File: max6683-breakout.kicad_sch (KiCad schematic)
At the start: 12 parts, among them J1 Conn_01x05, J2 Conn_01x05, U1 MAX6683

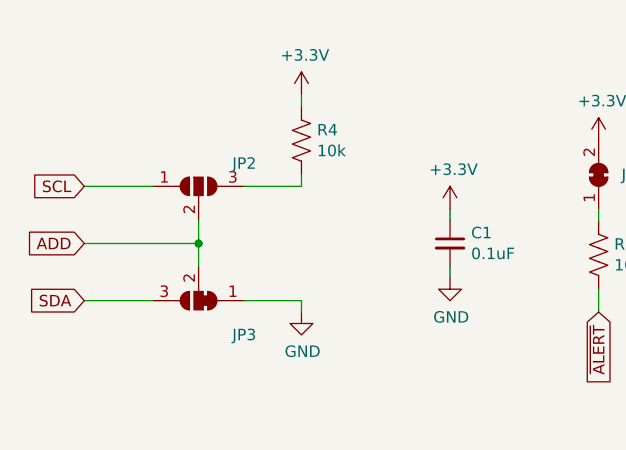
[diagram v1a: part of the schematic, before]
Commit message: Update PCB to eliminate clearance DRC issues
Supports #44.
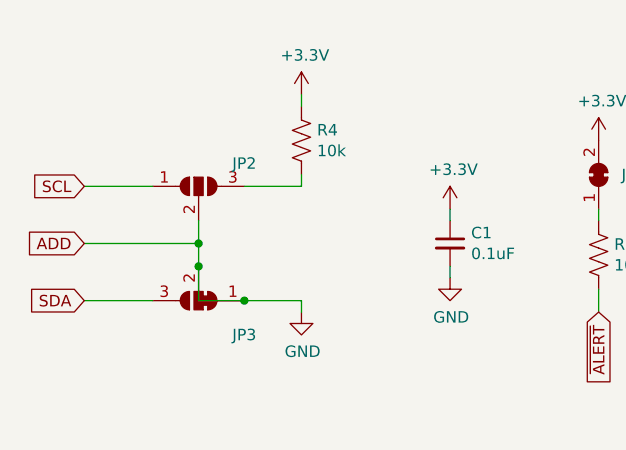
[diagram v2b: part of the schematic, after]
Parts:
- JP3: footprint Jumper:SolderJumper-3_P1.3mm_Bridged12_RoundedPad1.0x1.5mm -> Jumper:SolderJumper-3_P1.3mm_Open_RoundedPad1.0x1.5mm
- JP4: value (none) -> SolderJumper_2_Bridged; footprint (none) -> Jumper:SolderJumper-2_P1.3mm_Bridged_RoundedPad1.0x1.5mm
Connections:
- net ADD is gone; now on net GND: J2.2 (Pin_2), JP2.2 (C), JP3.2 (C), U1.7 (ADD)
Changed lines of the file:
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@@
   (junction (at 158.75 78.74) (diameter 0) (color 0 0 0 0)
   )
+  (junction (at 123.19 125.73) (diameter 0) (color 0 0 0 0)
+  )
   (junction (at 121.92 86.36) (diameter 0) (color 0 0 0 0)
+  )
+  (junction (at 118.11 121.92) (diameter 0) (color 0 0 0 0)
   )
   (no_connect (at 119.38 83.82))
@@
     (stroke (width 0) (type default) (color 0 0 0 0))
   )
+  (wire (pts (xy 118.11 125.73) (xy 118.11 121.92))
+    (stroke (width 0) (type default) (color 0 0 0 0))
+  )
   (wire (pts (xy 123.19 125.73) (xy 129.54 125.73))
     (stroke (width 0) (type default) (color 0 0 0 0))
@@
   )
   (wire (pts (xy 147.32 86.36) (xy 173.99 86.36))
+    (stroke (width 0) (type default) (color 0 0 0 0))
+  )
+  (wire (pts (xy 123.19 125.73) (xy 118.11 125.73))
     (stroke (width 0) (type default) (color 0 0 0 0))
   )
@@
       (effects (font (size 1.27 1.27)) hide)
     )
-    (property "Footprint" "Jumper:SolderJumper-3_P1.3mm_Bridged12_RoundedPad1.0x1.5mm" (id 2) (at 118.11 125.73 0)
+    (property "Footprint" "Jumper:SolderJumper-3_P1.3mm_Open_RoundedPad1.0x1.5mm" (id 2) (at 118.11 125.73 0)
       (effects (font (size 1.27 1.27)) hide)
     )
@@
       (effects (font (size 1.27 1.27)) (justify right))
     )
-    (property "Value" "" (id 1) (at 158.75 111.76 0)
-      (effects (font (size 1.27 1.27)) hide)
-    )
-    (property "Footprint" "" (id 2) (at 162.56 111.76 0)
+    (property "Value" "SolderJumper_2_Bridged" (id 1) (at 158.75 111.76 0)
+      (effects (font (size 1.27 1.27)) hide)
+    )
+    (property "Footprint" "Jumper:SolderJumper-2_P1.3mm_Bridged_RoundedPad1.0x1.5mm" (id 2) (at 162.56 111.76 0)
       (effects (font (size 1.27 1.27)) hide)
     )
@@
     )
     (path "/0fa81537-8214-4df6-96f6-9377354bc47f"
-      (reference "JP3") (unit 1) (value "SolderJumper_3_Bridged12") (footprint "Jumper:SolderJumper-3_P1.3mm_Bridged12_RoundedPad1.0x1.5mm")
+      (reference "JP3") (unit 1) (value "SolderJumper_3_Bridged12") (footprint "Jumper:SolderJumper-3_P1.3mm_Open_RoundedPad1.0x1.5mm")
     )
     (path "/18b6dcb6-5ab3-481b-b998-33e8cf6d281f"

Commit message: Begin routing
Supports #44.
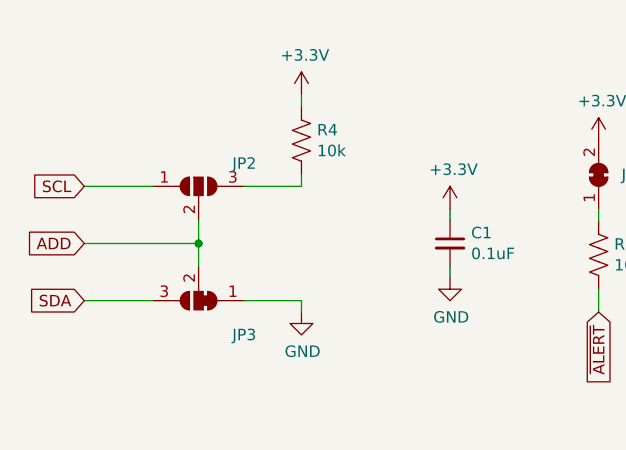
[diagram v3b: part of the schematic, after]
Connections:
- net GND: no longer J2.2 (Pin_2), JP2.2 (C), JP3.2 (C), U1.7 (ADD)
- new net ADD: J2.2 (Pin_2), JP2.2 (C), JP3.2 (C), U1.7 (ADD)
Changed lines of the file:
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@@
   (junction (at 158.75 78.74) (diameter 0) (color 0 0 0 0)
   )
-  (junction (at 123.19 125.73) (diameter 0) (color 0 0 0 0)
-  )
   (junction (at 121.92 86.36) (diameter 0) (color 0 0 0 0)
-  )
-  (junction (at 118.11 121.92) (diameter 0) (color 0 0 0 0)
   )
   (no_connect (at 119.38 83.82))
@@
     (stroke (width 0) (type default) (color 0 0 0 0))
   )
-  (wire (pts (xy 118.11 125.73) (xy 118.11 121.92))
-    (stroke (width 0) (type default) (color 0 0 0 0))
-  )
   (wire (pts (xy 123.19 125.73) (xy 129.54 125.73))
     (stroke (width 0) (type default) (color 0 0 0 0))
@@
     (stroke (width 0) (type default) (color 0 0 0 0))
   )
-  (wire (pts (xy 123.19 125.73) (xy 118.11 125.73))
-    (stroke (width 0) (type default) (color 0 0 0 0))
-  )

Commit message: Complete routing
Supports #44.
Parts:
- JP3: value SolderJumper_3_Bridged12 -> (none); footprint Jumper:SolderJumper-3_P1.3mm_Open_RoundedPad1.0x1.5mm -> (none)
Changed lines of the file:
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@@
     (in_bom no) (on_board yes)
     (property "Reference" "JP3" (id 0) (at 123.19 129.54 0))
-    (property "Value" "SolderJumper_3_Bridged12" (id 1) (at 118.11 129.54 0)
+    (property "Value" "" (id 1) (at 118.11 129.54 0)
       (effects (font (size 1.27 1.27)) hide)
     )
-    (property "Footprint" "Jumper:SolderJumper-3_P1.3mm_Open_RoundedPad1.0x1.5mm" (id 2) (at 118.11 125.73 0)
+    (property "Footprint" "" (id 2) (at 118.11 125.73 0)
       (effects (font (size 1.27 1.27)) hide)
     )
@@
     )
     (path "/0fa81537-8214-4df6-96f6-9377354bc47f"
-      (reference "JP3") (unit 1) (value "SolderJumper_3_Bridged12") (footprint "Jumper:SolderJumper-3_P1.3mm_Open_RoundedPad1.0x1.5mm")
+      (reference "JP3") (unit 1) (value "SolderJumper_3_Bridged12") (footprint "Jumper:SolderJumper-3_P1.3mm_Bridged12_RoundedPad1.0x1.5mm_NumberLabels")
     )
     (path "/18b6dcb6-5ab3-481b-b998-33e8cf6d281f"

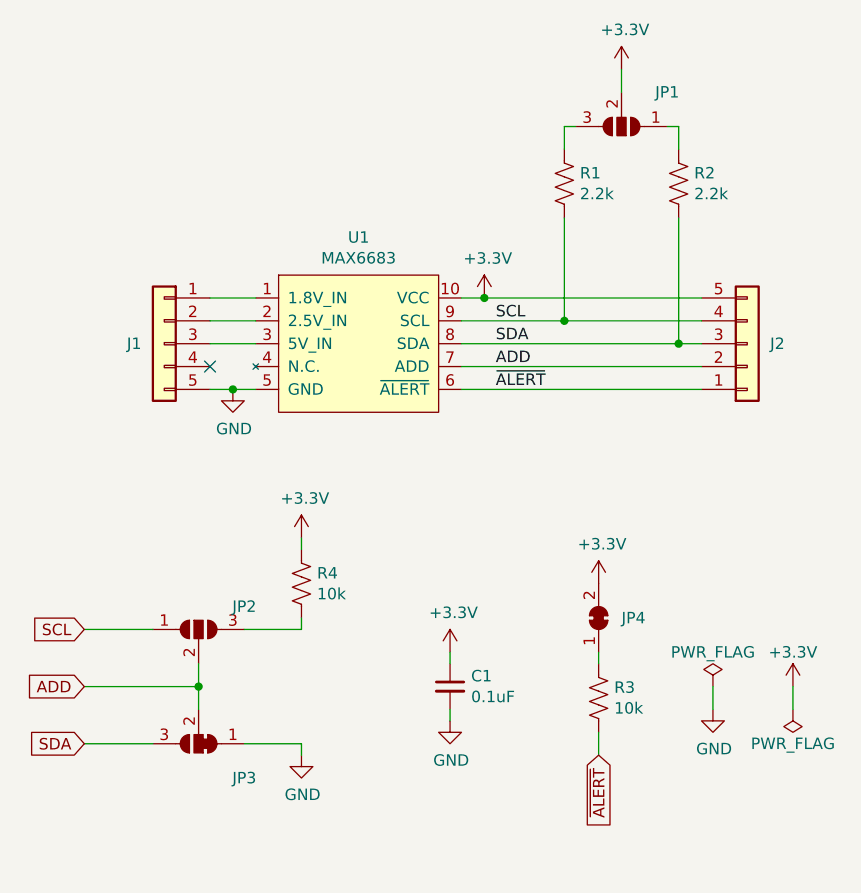
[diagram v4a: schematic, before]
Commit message: Inject ERC errors to test CI job
Supports #44.
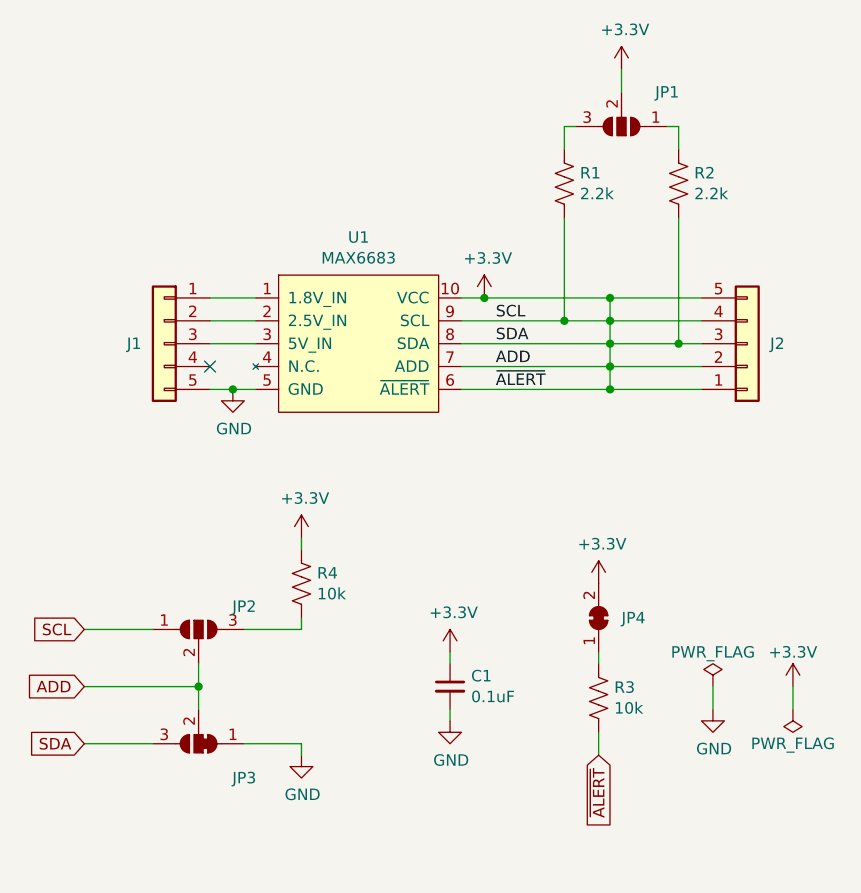
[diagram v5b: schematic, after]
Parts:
- JP3: value (none) -> SolderJumper_3_Bridged12; footprint (none) -> Jumper:SolderJumper-3_P1.3mm_Bridged12_RoundedPad1.0x1.5mm_NumberLabels
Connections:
- net ADD is gone; now on net +3V3: J2.2 (Pin_2), JP2.2 (C), JP3.2 (C), U1.7 (ADD)
- net SCL is gone; now on net +3V3: J2.4 (Pin_4), JP2.1 (A), R1.2, U1.9 (SCL)
- net SDA is gone; now on net +3V3: J2.3 (Pin_3), JP3.3 (B), R2.2, U1.8 (SDA)
- net ~{ALERT} is gone; now on net +3V3: J2.1 (Pin_1), R3.2, U1.6 (~{ALERT})
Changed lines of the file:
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@@
   (junction (at 171.45 81.28) (diameter 0) (color 0 0 0 0)
   )
+  (junction (at 163.83 76.2) (diameter 0) (color 0 0 0 0)
+  )
+  (junction (at 163.83 81.28) (diameter 0) (color 0 0 0 0)
+  )
   (junction (at 158.75 78.74) (diameter 0) (color 0 0 0 0)
   )
+  (junction (at 163.83 83.82) (diameter 0) (color 0 0 0 0)
+  )
+  (junction (at 163.83 78.74) (diameter 0) (color 0 0 0 0)
+  )
   (junction (at 121.92 86.36) (diameter 0) (color 0 0 0 0)
+  )
+  (junction (at 163.83 86.36) (diameter 0) (color 0 0 0 0)
   )
   (no_connect (at 119.38 83.82))
@@
     (stroke (width 0) (type default) (color 0 0 0 0))
   )
+  (wire (pts (xy 163.83 76.2) (xy 163.83 78.74))
+    (stroke (width 0) (type default) (color 0 0 0 0))
+  )
+  (wire (pts (xy 163.83 83.82) (xy 163.83 86.36))
+    (stroke (width 0) (type default) (color 0 0 0 0))
+  )
   (wire (pts (xy 121.92 86.36) (xy 124.46 86.36))
     (stroke (width 0) (type default) (color 0 0 0 0))
@@
     (stroke (width 0) (type default) (color 0 0 0 0))
   )
+  (wire (pts (xy 163.83 78.74) (xy 163.83 81.28))
+    (stroke (width 0) (type default) (color 0 0 0 0))
+  )
   (wire (pts (xy 119.38 76.2) (xy 124.46 76.2))
     (stroke (width 0) (type default) (color 0 0 0 0))
@@
     (stroke (width 0) (type default) (color 0 0 0 0))
   )
+  (wire (pts (xy 163.83 78.74) (xy 173.99 78.74))
+    (stroke (width 0) (type default) (color 0 0 0 0))
+  )
   (wire (pts (xy 162.56 115.57) (xy 162.56 116.84))
     (stroke (width 0) (type default) (color 0 0 0 0))
@@
     (stroke (width 0) (type default) (color 0 0 0 0))
   )
-  (wire (pts (xy 147.32 86.36) (xy 173.99 86.36))
-    (stroke (width 0) (type default) (color 0 0 0 0))
-  )
-  (wire (pts (xy 158.75 78.74) (xy 173.99 78.74))
+  (wire (pts (xy 163.83 86.36) (xy 173.99 86.36))
+    (stroke (width 0) (type default) (color 0 0 0 0))
+  )
+  (wire (pts (xy 163.83 81.28) (xy 171.45 81.28))
+    (stroke (width 0) (type default) (color 0 0 0 0))
+  )
+  (wire (pts (xy 147.32 86.36) (xy 163.83 86.36))
+    (stroke (width 0) (type default) (color 0 0 0 0))
+  )
+  (wire (pts (xy 163.83 83.82) (xy 173.99 83.82))
+    (stroke (width 0) (type default) (color 0 0 0 0))
+  )
+  (wire (pts (xy 158.75 78.74) (xy 163.83 78.74))
     (stroke (width 0) (type default) (color 0 0 0 0))
   )
@@
     (stroke (width 0) (type default) (color 0 0 0 0))
   )
-  (wire (pts (xy 149.86 76.2) (xy 173.99 76.2))
+  (wire (pts (xy 163.83 76.2) (xy 173.99 76.2))
+    (stroke (width 0) (type default) (color 0 0 0 0))
+  )
+  (wire (pts (xy 149.86 76.2) (xy 163.83 76.2))
     (stroke (width 0) (type default) (color 0 0 0 0))
   )
@@
     (stroke (width 0) (type default) (color 0 0 0 0))
   )
+  (wire (pts (xy 163.83 81.28) (xy 163.83 83.82))
+    (stroke (width 0) (type default) (color 0 0 0 0))
+  )
   (wire (pts (xy 165.1 50.8) (xy 165.1 53.34))
     (stroke (width 0) (type default) (color 0 0 0 0))
   )
-  (wire (pts (xy 147.32 83.82) (xy 173.99 83.82))
-    (stroke (width 0) (type default) (color 0 0 0 0))
-  )
-  (wire (pts (xy 147.32 81.28) (xy 171.45 81.28))
+  (wire (pts (xy 147.32 83.82) (xy 163.83 83.82))
+    (stroke (width 0) (type default) (color 0 0 0 0))
+  )
+  (wire (pts (xy 147.32 81.28) (xy 163.83 81.28))
     (stroke (width 0) (type default) (color 0 0 0 0))
   )
@@
     (in_bom no) (on_board yes)
     (property "Reference" "JP3" (id 0) (at 123.19 129.54 0))
-    (property "Value" "" (id 1) (at 118.11 129.54 0)
-      (effects (font (size 1.27 1.27)) hide)
-    )
-    (property "Footprint" "" (id 2) (at 118.11 125.73 0)
-      (effects (font (size 1.27 1.27)) hide)
-    )
+    (property "Value" "SolderJumper_3_Bridged12" (id 1) (at 118.11 129.54 0)
+      (effects (font (size 1.27 1.27)) hide)
+    )
+    (property "Footprint" "Jumper:SolderJumper-3_P1.3mm_Bridged12_RoundedPad1.0x1.5mm_NumberLabels" (id 2) (at 118.11 125.73 0)
+      (effects (font (size 1.27 1.27)) hide)
+    )

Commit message: Remove intentional ERC errors
Supports #44.
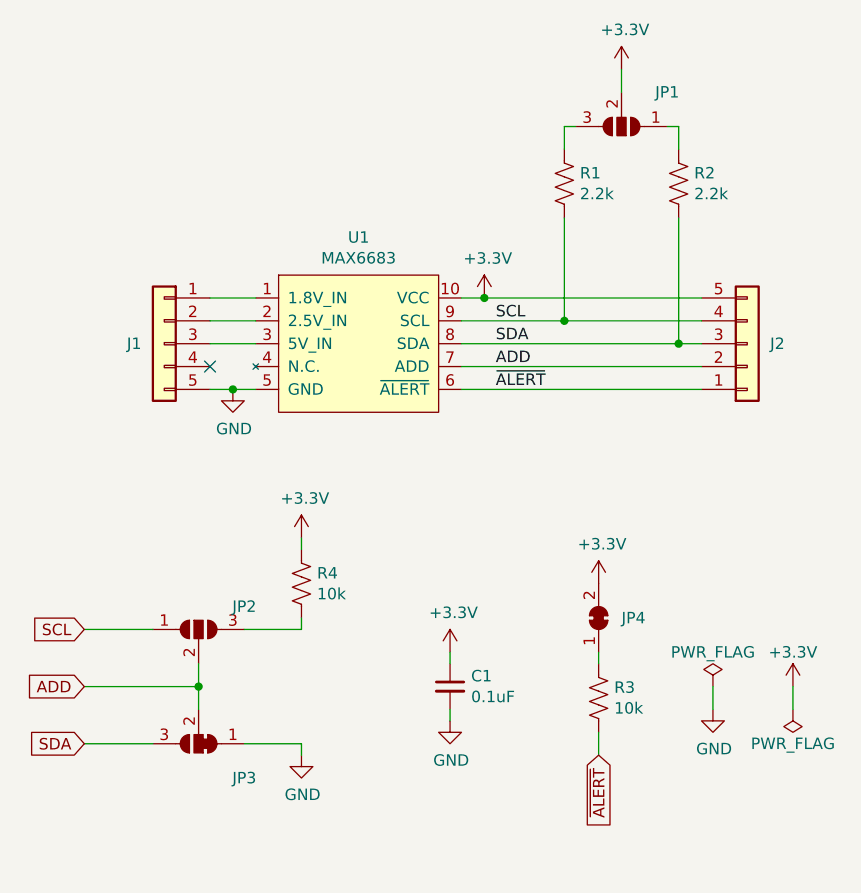
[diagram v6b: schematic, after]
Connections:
- net +3V3: no longer J2.1 (Pin_1), J2.2 (Pin_2), J2.3 (Pin_3), J2.4 (Pin_4), JP2.1 (A), JP2.2 (C), JP3.2 (C), JP3.3 (B), R1.2, R2.2, R3.2, U1.6 (~{ALERT}), U1.7 (ADD), U1.8 (SDA), U1.9 (SCL)
- new net ADD: J2.2 (Pin_2), JP2.2 (C), JP3.2 (C), U1.7 (ADD)
- new net SCL: J2.4 (Pin_4), JP2.1 (A), R1.2, U1.9 (SCL)
- new net SDA: J2.3 (Pin_3), JP3.3 (B), R2.2, U1.8 (SDA)
- new net ~{ALERT}: J2.1 (Pin_1), R3.2, U1.6 (~{ALERT})
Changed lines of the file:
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@@
   (junction (at 171.45 81.28) (diameter 0) (color 0 0 0 0)
-  )
-  (junction (at 163.83 76.2) (diameter 0) (color 0 0 0 0)
-  )
-  (junction (at 163.83 81.28) (diameter 0) (color 0 0 0 0)
   )
   (junction (at 158.75 78.74) (diameter 0) (color 0 0 0 0)
   )
-  (junction (at 163.83 83.82) (diameter 0) (color 0 0 0 0)
-  )
-  (junction (at 163.83 78.74) (diameter 0) (color 0 0 0 0)
-  )
   (junction (at 121.92 86.36) (diameter 0) (color 0 0 0 0)
-  )
-  (junction (at 163.83 86.36) (diameter 0) (color 0 0 0 0)
   )
   (no_connect (at 119.38 83.82))
@@
     (stroke (width 0) (type default) (color 0 0 0 0))
   )
-  (wire (pts (xy 163.83 76.2) (xy 163.83 78.74))
-    (stroke (width 0) (type default) (color 0 0 0 0))
-  )
-  (wire (pts (xy 163.83 83.82) (xy 163.83 86.36))
-    (stroke (width 0) (type default) (color 0 0 0 0))
-  )
   (wire (pts (xy 121.92 86.36) (xy 124.46 86.36))
     (stroke (width 0) (type default) (color 0 0 0 0))
@@
     (stroke (width 0) (type default) (color 0 0 0 0))
   )
-  (wire (pts (xy 163.83 78.74) (xy 163.83 81.28))
-    (stroke (width 0) (type default) (color 0 0 0 0))
-  )
   (wire (pts (xy 119.38 76.2) (xy 124.46 76.2))
     (stroke (width 0) (type default) (color 0 0 0 0))
@@
     (stroke (width 0) (type default) (color 0 0 0 0))
   )
-  (wire (pts (xy 163.83 78.74) (xy 173.99 78.74))
-    (stroke (width 0) (type default) (color 0 0 0 0))
-  )
   (wire (pts (xy 162.56 115.57) (xy 162.56 116.84))
     (stroke (width 0) (type default) (color 0 0 0 0))
@@
     (stroke (width 0) (type default) (color 0 0 0 0))
   )
-  (wire (pts (xy 163.83 86.36) (xy 173.99 86.36))
+  (wire (pts (xy 147.32 86.36) (xy 173.99 86.36))
     (stroke (width 0) (type default) (color 0 0 0 0))
   )
-  (wire (pts (xy 163.83 81.28) (xy 171.45 81.28))
-    (stroke (width 0) (type default) (color 0 0 0 0))
-  )
-  (wire (pts (xy 147.32 86.36) (xy 163.83 86.36))
-    (stroke (width 0) (type default) (color 0 0 0 0))
-  )
-  (wire (pts (xy 163.83 83.82) (xy 173.99 83.82))
-    (stroke (width 0) (type default) (color 0 0 0 0))
-  )
-  (wire (pts (xy 158.75 78.74) (xy 163.83 78.74))
+  (wire (pts (xy 158.75 78.74) (xy 173.99 78.74))
     (stroke (width 0) (type default) (color 0 0 0 0))
   )
@@
     (stroke (width 0) (type default) (color 0 0 0 0))
   )
-  (wire (pts (xy 163.83 76.2) (xy 173.99 76.2))
-    (stroke (width 0) (type default) (color 0 0 0 0))
-  )
-  (wire (pts (xy 149.86 76.2) (xy 163.83 76.2))
+  (wire (pts (xy 149.86 76.2) (xy 173.99 76.2))
     (stroke (width 0) (type default) (color 0 0 0 0))
   )
@@
     (stroke (width 0) (type default) (color 0 0 0 0))
   )
-  (wire (pts (xy 163.83 81.28) (xy 163.83 83.82))
-    (stroke (width 0) (type default) (color 0 0 0 0))
-  )
   (wire (pts (xy 165.1 50.8) (xy 165.1 53.34))
     (stroke (width 0) (type default) (color 0 0 0 0))
   )
-  (wire (pts (xy 147.32 83.82) (xy 163.83 83.82))
+  (wire (pts (xy 147.32 83.82) (xy 173.99 83.82))
     (stroke (width 0) (type default) (color 0 0 0 0))
   )
-  (wire (pts (xy 147.32 81.28) (xy 163.83 81.28))
+  (wire (pts (xy 147.32 81.28) (xy 171.45 81.28))
     (stroke (width 0) (type default) (color 0 0 0 0))
   )
